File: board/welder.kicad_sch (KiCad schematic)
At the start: 19 parts, among them J1 48 VDC INPUT, Q1 Q_NIGBT_GCE, Q2 Q_NIGBT_GCE, Q3 Q_NIGBT_GCE, Q4 Q_NIGBT_GCE, U1 RPMH15-0.5, U2 R-78E3.3-0.5, U3 MIC4604YM, U4 MIC4604YM

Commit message: updated filter simulation
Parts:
- Q1, Q2, Q3, Q4: MFG1 (none) -> Microchip; MFG1PN (none) -> APT95GR65B2
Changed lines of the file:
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@@
+      (effects (font (size 1.27 1.27)) hide)
+    )
+    (property "MFG1" "Microchip" (id 4) (at 158.75 57.15 0)
+      (effects (font (size 1.27 1.27)) hide)
+    )
+    (property "MFG1PN" "APT95GR65B2" (id 5) (at 158.75 57.15 0)
       (effects (font (size 1.27 1.27)) hide)
     )
@@
       (effects (font (size 1.27 1.27)) hide)
     )
+    (property "MFG1" "Microchip" (id 4) (at 158.75 105.41 0)
+      (effects (font (size 1.27 1.27)) hide)
+    )
+    (property "MFG1PN" "APT95GR65B2" (id 5) (at 158.75 105.41 0)
+      (effects (font (size 1.27 1.27)) hide)
+    )
     (pin "1")
     (pin "2")
@@
     )
     (property "Datasheet" "~" (id 3) (at 158.75 92.71 0)
+      (effects (font (size 1.27 1.27)) hide)
+    )
+    (property "MFG1" "Microchip" (id 4) (at 158.75 92.71 0)
+      (effects (font (size 1.27 1.27)) hide)
+    )
+    (property "MFG1PN" "APT95GR65B2" (id 5) (at 158.75 92.71 0)
       (effects (font (size 1.27 1.27)) hide)
     )
@@
       (effects (font (size 1.27 1.27)) hide)
     )
+    (property "MFG1" "Microchip" (id 4) (at 158.75 44.45 0)
+      (effects (font (size 1.27 1.27)) hide)
+    )
+    (property "MFG1PN" "APT95GR65B2" (id 5) (at 158.75 44.45 0)
+      (effects (font (size 1.27 1.27)) hide)
+    )

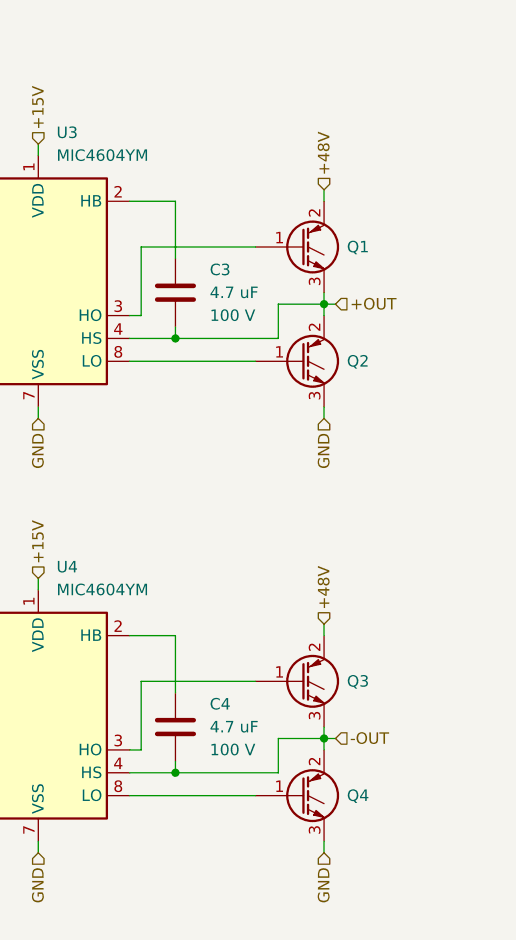
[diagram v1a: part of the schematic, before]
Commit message: Add fw diodes
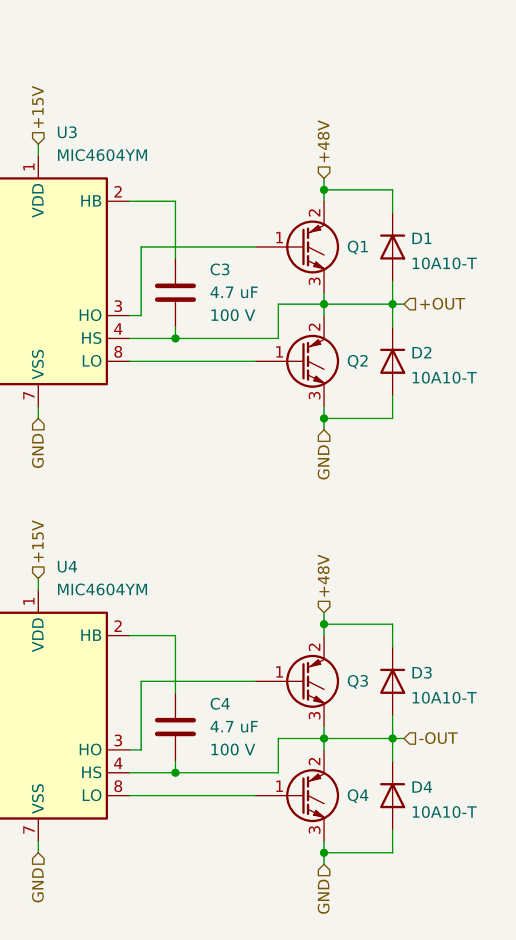
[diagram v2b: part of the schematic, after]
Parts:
- added D1, D2, D3, D4: 10A10-T, Diode_THT:D_P600_R-6_P7.62mm_Vertical_AnodeUp, symbol Device:D
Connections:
- net +48V: now also D1.1 (K), D3.1 (K)
- net +OUT: now also D1.2 (A), D2.1 (K)
- net -OUT: now also D3.2 (A), D4.1 (K)
- net GND: now also D2.2 (A), D4.2 (A)

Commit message: Added a bunch of stuff to schematic
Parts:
- removed C5: 2.2 uF, symbol Device:C
- removed C7: 10 uF, symbol Device:C
- removed C9: 22 uF, symbol Device:C
- removed L1: 12 uH, Inductor_SMD:L_Bourns_SRN6045TA, symbol Device:L
- removed U1: RPMH15-0.5, Converter_DCDC:Converter_DCDC_RECOM_RPMx.x-x.0, symbol Converter_DCDC:RPM5.0-3.0
- added C? (x3): 0.1 uF, Capacitor_SMD:C_0603_1608Metric, symbol Device:C
- added C? (x2): 10 uF, Capacitor_SMD:C_0603_1608Metric, symbol Device:C
- added C? (x5): 0.1uF, Capacitor_SMD:C_0603_1608Metric, symbol Device:C
- added C? (x2): 47 pF, Capacitor_SMD:C_0603_1608Metric, symbol Device:C
- added C?: 47 uF, symbol Device:C
- added C?: 1 uF, Capacitor_SMD:C_0603_1608Metric, symbol Device:C
- added C? (x2): 0.1 uF, symbol Device:C
- added D?: FML340A-W, Diode_SMD:D_SMA, symbol Device:D_Schottky
- added FB?: Ferrite_Bead, Inductor_SMD:L_0603_1608Metric, symbol cat-tracker-board-rescue:Ferrite_Bead-Device
- added J?: Conn_01x10, Connector_PinHeader_1.27mm:PinHeader_2x05_P1.27mm_Horizontal, symbol Connector_Generic:Conn_01x10
- added J?: USB_B, HotMeltTechnologies:USB_B_AMPHENOL_P-UE27-BCX4-XXX_Horizontal, symbol Connector:USB_B
- added J?: Barrel_Jack_Switch, Connector_BarrelJack:BarrelJack_Horizontal, symbol Connector:Barrel_Jack_Switch
- added J?: POS, symbol Connector_Generic:Conn_01x01
- added J?: NEG, symbol Connector_Generic:Conn_01x01
- added L?: 20 uH, symbol Device:L
- added R? (x2): 100k, Resistor_SMD:R_0603_1608Metric, symbol Device:R
- added R?: 100 u, symbol Device:R
- added U?: ATSAMD21E18A-A, Package_QFP:TQFP-32_7x7mm_P0.8mm, symbol MCU_Microchip_SAMD:ATSAMD21E18A-A
- added U? (x7): 74LS04, symbol 74xx:74LS04
- added U? (x5): 74LS08, symbol 74xx:74LS08
- added U?: FT232RL, Package_SO:SSOP-28_5.3x10.2mm_P0.65mm, symbol Interface_USB:FT232RL
- added U?: INA240A3D, Package_SO:SOIC-8_3.9x4.9mm_P1.27mm, symbol Amplifier_Current:INA240A3D
- added U?: R-78E5.0-0.5, Converter_DCDC:Converter_DCDC_RECOM_R-78E-0.5_THT, symbol Regulator_Switching:R-78E5.0-0.5
- U2: value R-78E3.3-0.5 -> mEZD71201A-F; MFG1 (none) -> Monolithic Power Systems; MFG1PN (none) -> mEZD71201A-F
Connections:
- net +15V: now also C?.1, J?.1, U?.1 (IN); no longer C6.1, U2.1 (IN)
- net +3V3: now also C?.1, C?.1, C?.1, C?.2, FB?.1, J?.1 (Pin_1), R?.1, R?.1, U?.3 (REF2), U?.30 (VDDIN), U?.4 (VCCIO), U?.6 (V+)
- net GND: now also C?.1, C?.1, C?.1, C?.2, C?.2, C?.2, C?.2, C?.2, C?.2, C?.2, C?.2, C?.2, C?.2, C?.2, C?.2, J?.2, J?.3 (Pin_3), J?.4 (GND), J?.5 (Pin_5), J?.5 (Shield), U?.10, U?.10 (GND), U?.11, U?.12, U?.13, U?.13, U?.18 (GND), U?.2 (GND), U?.2 (GND), U?.21 (GND), U?.25 (AGND), U?.26 (TEST), U?.28 (GND), U?.4 (GND), U?.7 (GND), U?.7 (GND), U?.7 (GND), U?.7 (REF1), U?.9, U?.9
- net B: now reaches U4.5 (HI)
- net B: now also U?.3, U?.6
- net at U4.6 (LI): now also U?.4
- net A: now reaches U3.5 (HI)
- net A: now also U?.1, U?.3
- net at U3.6 (LI): now also U?.2
- net +OUT: no longer names the net of C3.1, D1.2 (A), D2.1 (K), Q1.3 (E), Q2.2 (C), U3.4 (HS)
- net +OUT: now also L?.1
- net -OUT renamed SENSE-
- net SENSE-: now also R?.1, U?.1 (-)
- new net: C?.2, U?.29 (VDDCORE)
- new net: C?.1, C?.2, FB?.2, U?.9 (VDDANA)
- new net: C?.1, U?.17 (3V3OUT)
- new net: C?.1, J?.3 (D+), U?.15 (USBD+)
- new net: D?.2 (A), J?.1 (VBUS)
- new net: C?.1, J?.2 (D-), U?.16 (USBD-)
- new net: U?.5, U?.6
- new net: C?.1, J?.1 (Pin_1), L?.2
- new net +5V: C6.1, C?.1, C?.1, C?.1, C?.1, D?.1 (K), U2.1 (IN), U?.14 (VCC), U?.14 (VCC), U?.19 (~{RESET}), U?.20 (VCC), U?.3 (OUT)
- new net POLARITY: U?.2, U?.5, U?.7 (PA06)
- new net PWM: U?.1, U?.4, U?.5 (PA04)
- new net RX: U?.1 (TXD), U?.12 (PA09)
- new net SENSE: U?.3 (PA02), U?.5
- new net SENSE+: C?.2, J?.1 (Pin_1), R?.2, U?.8 (+)
- new net SWCLK: J?.4 (Pin_4), R?.2, U?.31 (PA30)
- new net SWDIO: J?.2 (Pin_2), U?.32 (PA31)
- new net TX: U?.11 (PA08), U?.5 (RXD)
- new net nRESET: J?.10 (Pin_10), R?.2, U?.26 (~{RESET})
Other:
- note added: "Rshunt: 100 uOhm Ishunt: [-165, 165] A Vshunt: [-16.5, 16.5] mV gain: 100 V/V Vout: [0, 3.3] V"
- moved on the sheet: C1, C2, C3, C4, C6, C8, D1, D2, D3, D4, Q1, Q2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

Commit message: Add pwm, pol truth table
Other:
- note added: "PWM POL AH AL BH BL 0 X 0 0 0 0 1 1 1 0 0 1 1 0 0 1 1 0"
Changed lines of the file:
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@@
     (stroke (width 0) (type default) (color 0 0 0 0))
+  )
+  (text "PWM	POL	AH	AL	BH	BL\n0	X	0	0	0	0\n1	1	1	0	0	1\n1	0	0	1	1	0"
+    (at 210.82 66.04 0)
+    (effects (font (size 1.27 1.27)) (justify left bottom))
   )
   (text "Rshunt: 100 uOhm\nIshunt: [-165, 165] A\nVshunt: [-16.5, 16.5] mV\ngain: 100 V/V\nVout: [0, 3.3] V"

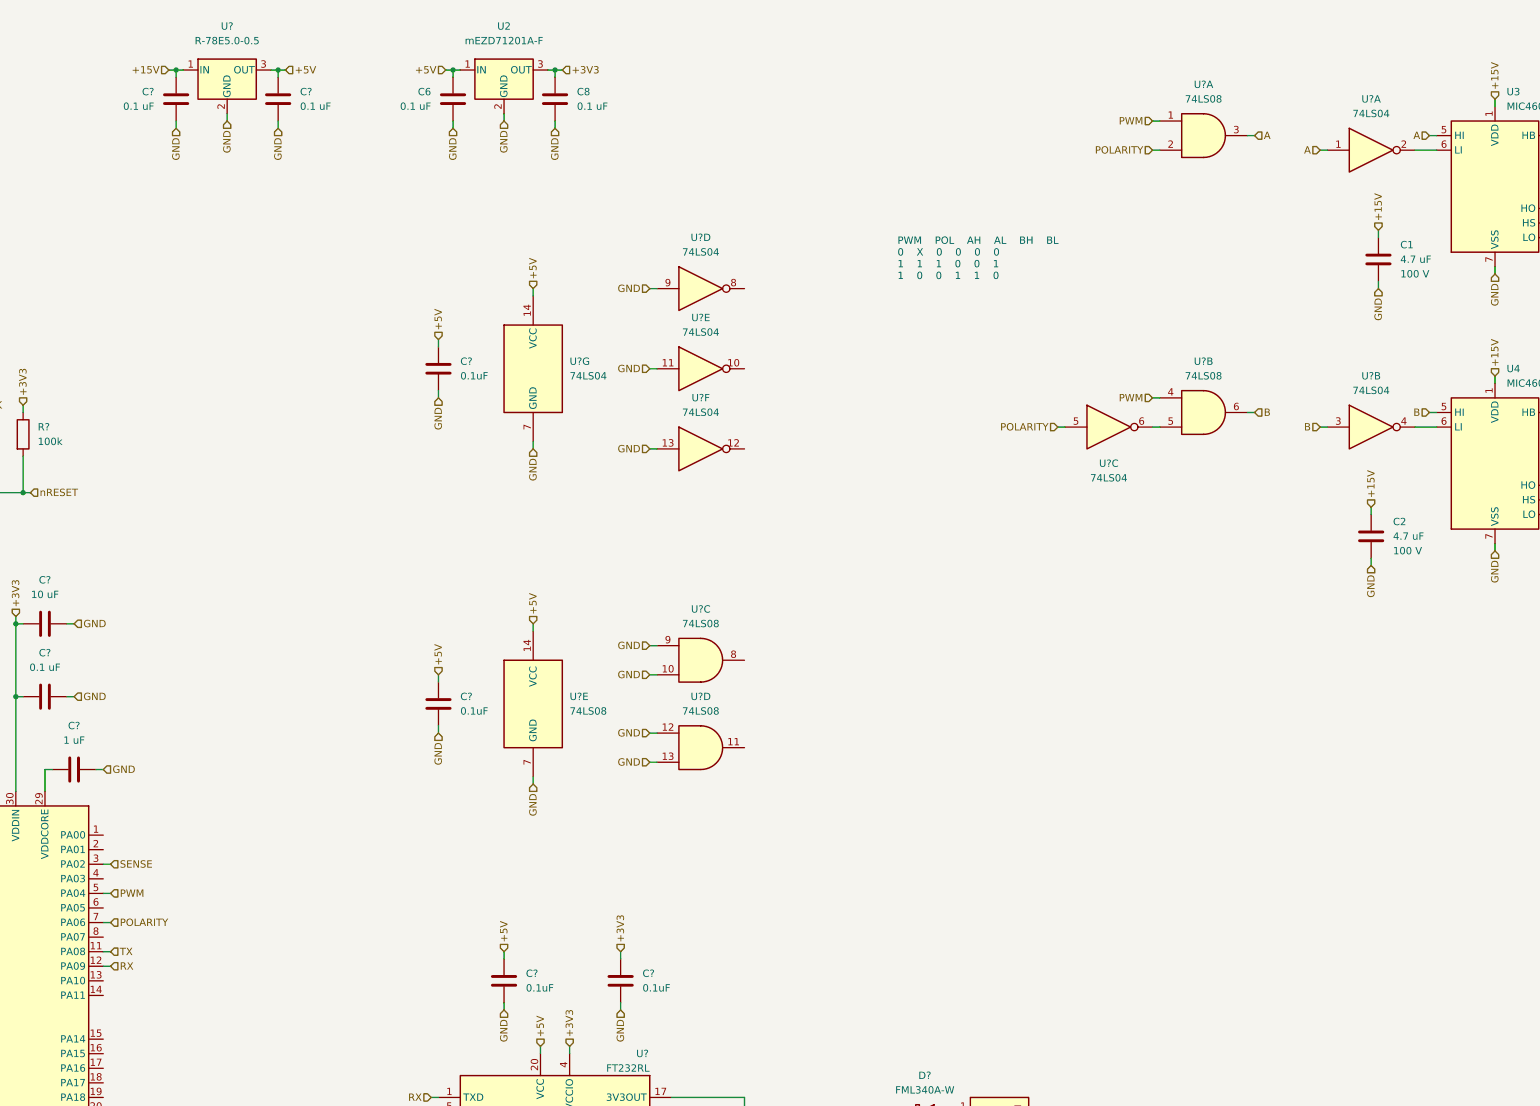
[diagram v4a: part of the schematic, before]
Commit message: Removed logic chips, it can be done in the SAM
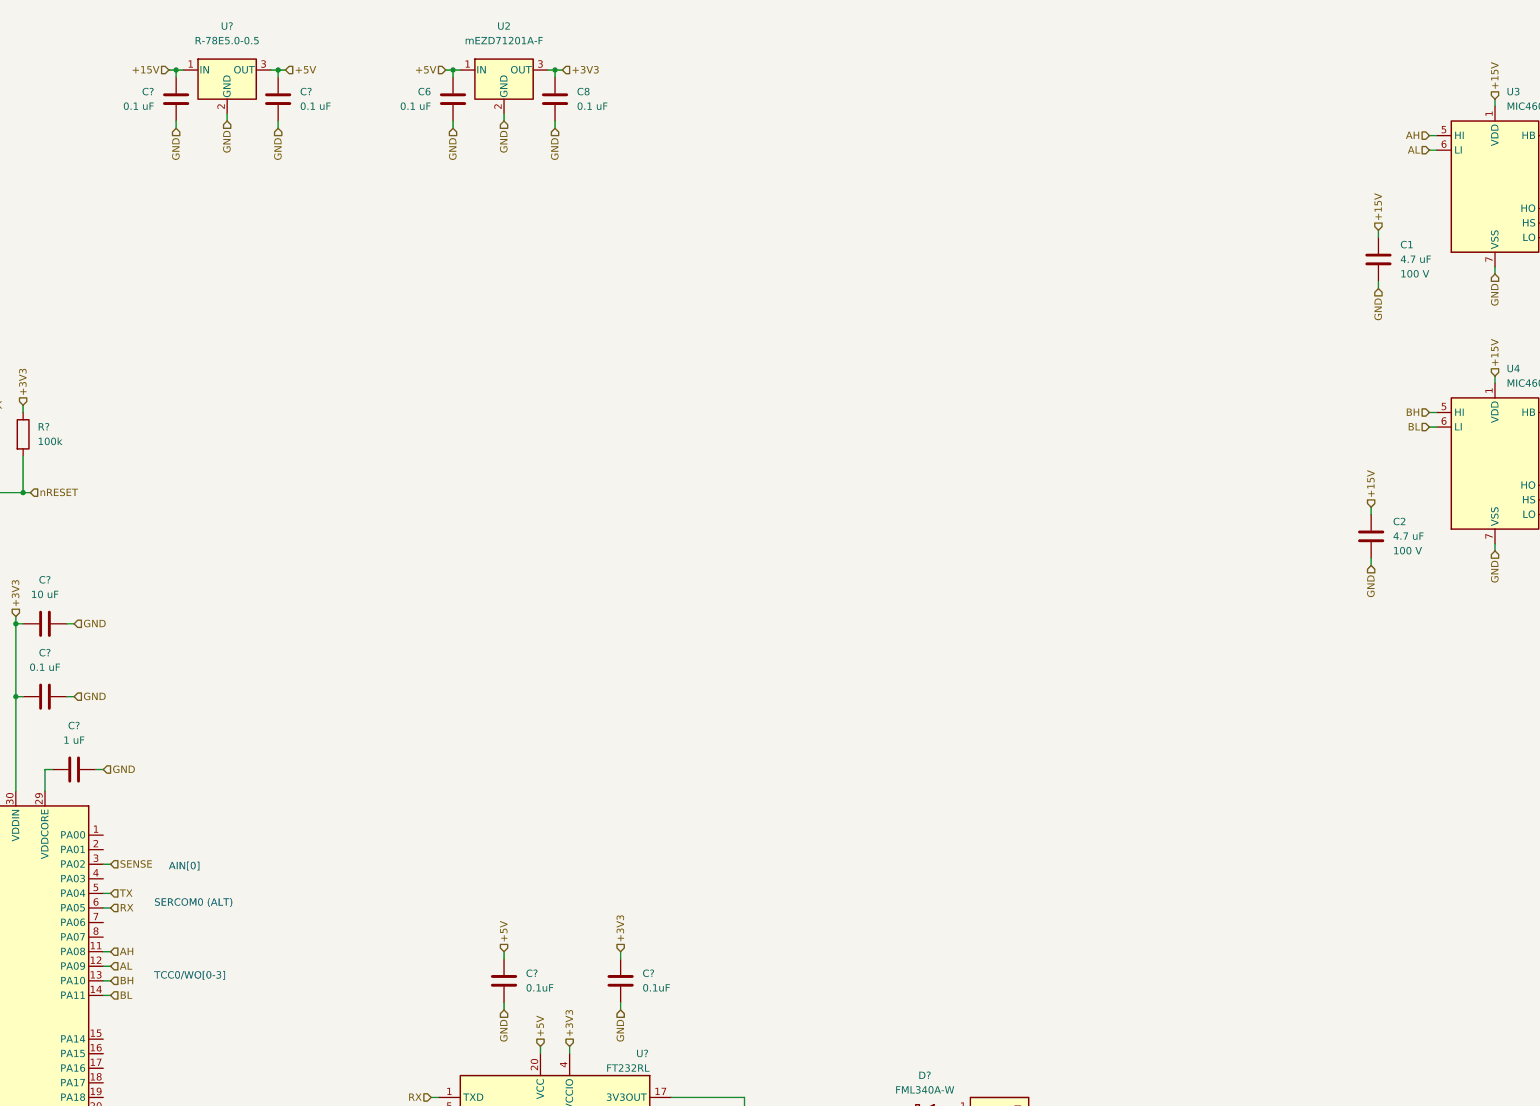
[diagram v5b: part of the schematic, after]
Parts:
- removed C? (x2): 0.1uF, Capacitor_SMD:C_0603_1608Metric, symbol Device:C
- removed U? (x7): 74LS04, symbol 74xx:74LS04
- removed U? (x5): 74LS08, symbol 74xx:74LS08
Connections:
- net B is gone; now on net BH: U4.5 (HI)
- net PWM is gone; now on net TX: U?.5 (PA04)
- net RX: now also U?.6 (PA05); no longer U?.12 (PA09)
- net TX: no longer U?.11 (PA08)
- net BH: now reaches U?.13 (PA10)
- net BL: now reaches U?.14 (PA11)
- net BL: now also U4.6 (LI)
- net AL: now reaches U3.6 (LI)
- net AL: now also U?.12 (PA09)
- net A renamed AH
- net AH: now also U?.11 (PA08)
- net POLARITY: no longer names the net of U?.7 (PA06)
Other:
- note added: "AIN[0]"
- note added: "SERCOM0 (ALT)"
- note added: "TCC0/WO[0-3]"
- note removed: "PWM POL AH AL BH BL 0 X 0 0 0 0 1 1 1 0 0 1 1 0 0 1 1 0"
